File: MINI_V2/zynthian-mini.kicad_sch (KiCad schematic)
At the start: 88 parts, among them J1 NEUTRIK, J2 NEUTRIK, J3 Conn_02x04_Odd_Even, J4 Conn_01x05, J6 TRRS-PJ-320A, SW1 SW_Push, SW10 SW_Push, SW11 SW_Push, SW12 SW_Push, SW13 SW_Push, SW14 SW_Push, SW15 SW_Push, SW16 SW_Push, SW17 SW_Push, SW18 SW_Push, SW19 SW_Push, SW2 SW_Push, SW20 SW_Push, SW3 SW_Push, SW4 SW_Push, SW5 SW_Push, SW6 SW_Push, SW7 SW_Push, SW8 SW_Push, SW9 SW_Push, U1 74HCT14, U2 H11L1M

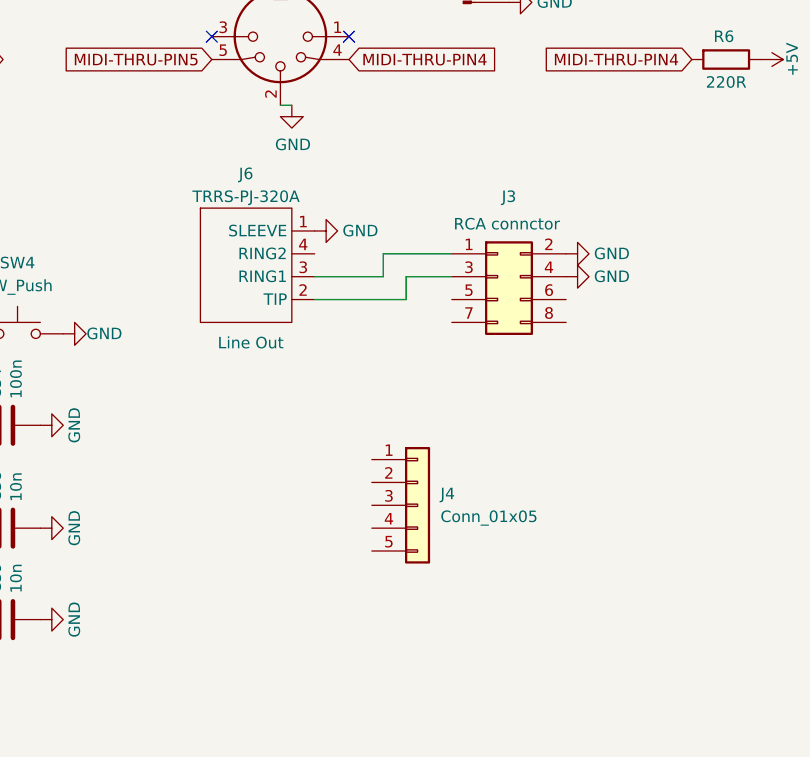
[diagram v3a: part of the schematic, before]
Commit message: small cleanup for old traces, add 2nd mini jack
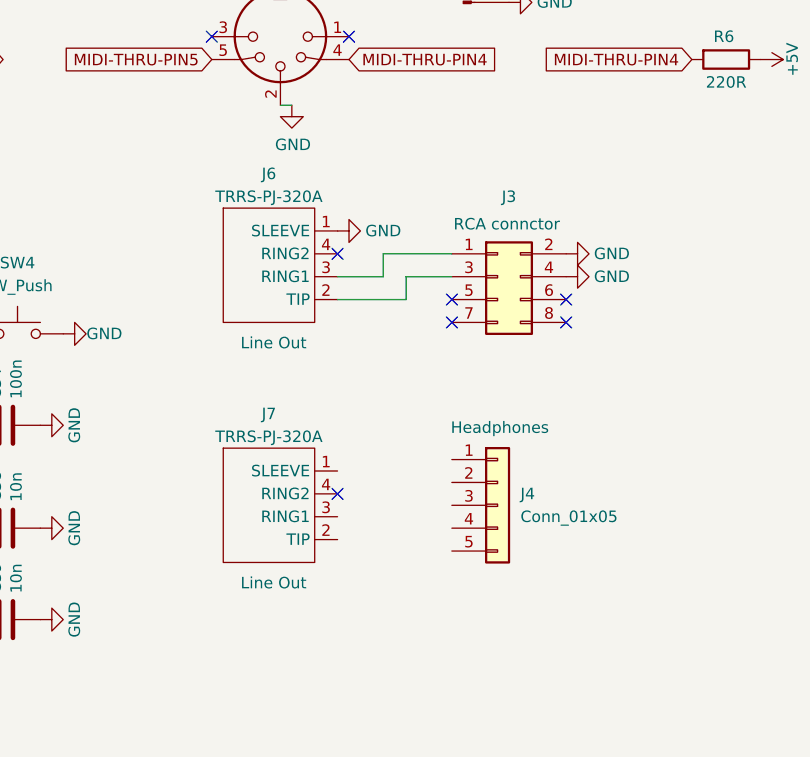
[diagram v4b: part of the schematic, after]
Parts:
- added J7: TRRS-PJ-320A, project-footprints:TRRS-PJ-320A, symbol TRRS_jack:TRRS-PJ-320A
- J4: Comment (none) -> Headphones
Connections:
- no-connect marks 15 -> 21
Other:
- moved on the sheet: J4, J6
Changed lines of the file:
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@@
 	)
 	(no_connect
+		(at 309.88 123.19)
+	)
+	(no_connect
 		(at 285.75 41.91)
 	)
@@
 	)
 	(no_connect
+		(at 322.58 123.19)
+	)
+	(no_connect
+		(at 297.18 115.57)
+	)
+	(no_connect
 		(at 22.86 160.02)
 	)
@@
 	)
 	(no_connect
+		(at 322.58 120.65)
+	)
+	(no_connect
 		(at 372.11 26.67)
 	)
 	(no_connect
+		(at 309.88 120.65)
+	)
+	(no_connect
+		(at 297.18 142.24)
+	)
+	(no_connect
 		(at 278.13 34.29)
 	)
@@
 	(wire
 		(pts
-			(xy 304.8 120.65) (xy 294.64 120.65)
+			(xy 304.8 120.65) (xy 297.18 120.65)
 		)
 		(stroke
@@
 	(wire
 		(pts
-			(xy 302.26 118.11) (xy 294.64 118.11)
+			(xy 302.26 118.11) (xy 297.18 118.11)
 		)
 		(stroke
@@
 	)
 	(symbol
+		(lib_id "TRRS_jack:TRRS-PJ-320A")
+		(at 289.56 143.51 0)
+		(unit 1)
+		(exclude_from_sim no)
+		(in_bom yes)
+		(on_board yes)
+		(dnp no)
+		(property "Reference" "J7"
+			(at 289.56 133.35 0)
+			(effects
+				(font
+					(size 1.27 1.27)
+				)
+			)
+		)
+		(property "Value" "TRRS-PJ-320A"
+			(at 289.56 135.89 0)
+			(effects
+				(font
+					(size 1.27 1.27)
+				)
+			)
+		)
+		(property "Footprint" "project-footprints:TRRS-PJ-320A"
+			(at 289.56 143.51 0)
+			(effects
+				(font
+					(size 1.27 1.27)
+				)
+				(hide yes)
+			)
+		)
+		(property "Datasheet" ""
+			(at 289.56 143.51 0)
+			(effects
+				(font
+					(size 1.27 1.27)
+				)
+				(hide yes)
+			)
+		)
+		(property "Description" ""
+			(at 289.56 143.51 0)
+			(effects
+				(font
+					(size 1.27 1.27)
+				)
+				(hide yes)
+			)
+		)
+		(property "MPN" "TRRS-PJ-320A"
+			(at 289.56 143.51 0)
+			(effects
+				(font
+					(size 1.27 1.27)
+				)
+				(hide yes)
+			)
+		)
+		(property "Link" "https://keycapsss.com/keyboard-parts/parts/54/2x-trrs-jacks-3.5mm"
+			(at 289.56 143.51 0)
+			(effects
+				(font
+					(size 1.27 1.27)
+				)
+				(hide yes)
+			)
+		)
+		(property "Comment" "Line Out"
+			(at 290.068 152.146 0)
+			(effects
+				(font
+					(size 1.27 1.27)
+				)
+			)
+		)
+		(pin "4"
+		)
+		(pin "3"
+		)
+		(pin "2"
+		)
+		(pin "1"
+		)
+		(instances
+			(project "zynthian-mini"
+				(path "/2377c5bc-c72f-48a3-b88d-9704bbbe65db"
+					(reference "J7")
+					(unit 1)
+				)
+			)
+		)
+	)
+	(symbol
 		(lib_id "power:GND")
 		(at 246.38 267.97 90)
@@
 	(symbol
 		(lib_id "TRRS_jack:TRRS-PJ-320A")
-		(at 287.02 116.84 0)
+		(at 289.56 116.84 0)
 		(unit 1)
 		(exclude_from_sim no)
@@
 		(dnp no)
 		(property "Reference" "J6"
-			(at 287.02 106.68 0)
+			(at 289.56 106.68 0)
 			(effects
 				(font
@@
 		)
 		(property "Value" "TRRS-PJ-320A"
-			(at 287.02 109.22 0)
+			(at 289.56 109.22 0)
 			(effects
 				(font
@@
 		)
 		(property "Footprint" "project-footprints:TRRS-PJ-320A"
-			(at 287.02 116.84 0)
+			(at 289.56 116.84 0)
 			(effects
 				(font
@@
 		)
 		(property "Datasheet" ""
-			(at 287.02 116.84 0)
+			(at 289.56 116.84 0)
 			(effects
 				(font
@@
 		)
 		(property "Description" ""
-			(at 287.02 116.84 0)
+			(at 289.56 116.84 0)
 			(effects
 				(font
@@
 		)
 		(property "MPN" "TRRS-PJ-320A"
-			(at 287.02 116.84 0)
+			(at 289.56 116.84 0)
 			(effects
 				(font
@@
 		)
 		(property "Link" "https://keycapsss.com/keyboard-parts/parts/54/2x-trrs-jacks-3.5mm"
-			(at 287.02 116.84 0)
+			(at 289.56 116.84 0)
 			(effects
 				(font
@@
 		)
 		(property "Comment" "Line Out"
-			(at 287.528 125.476 0)
+			(at 290.068 125.476 0)
 			(effects
 				(font
@@
 	(symbol
 		(lib_id "power:GND")
-		(at 294.64 113.03 90)
+		(at 297.18 113.03 90)
 		(mirror x)
 		(unit 1)
@@
 		(dnp no)
 		(property "Reference" "#PWR077"
-			(at 300.99 113.03 0)
+			(at 303.53 113.03 0)
 			(effects
 				(font
@@
 		)
 		(property "Value" "GND"
-			(at 299.72 113.03 90)
+			(at 302.26 113.03 90)
 			(effects
 				(font
@@
 		)
 		(property "Footprint" ""
-			(at 294.64 113.03 0)
+			(at 297.18 113.03 0)
 			(effects
 				(font
@@
 		)
 		(property "Datasheet" ""
-			(at 294.64 113.03 0)
+			(at 297.18 113.03 0)
 			(effects
 				(font
@@
 		)
 		(property "Description" "Power symbol creates a global label with name \"GND\" , ground"
-			(at 294.64 113.03 0)
+			(at 297.18 113.03 0)
 			(effects
 				(font
@@
 	(symbol
 		(lib_id "Connector_Generic:Conn_01x05")
-		(at 306.07 143.51 0)
+		(at 314.96 143.51 0)
 		(unit 1)
 		(exclude_from_sim no)
@@
 		(on_board yes)
 		(dnp no)
-		(fields_autoplaced yes)
 		(property "Reference" "J4"
-			(at 308.61 142.2399 0)
+			(at 317.5 142.2399 0)
 			(effects
 				(font
@@
 		)
 		(property "Value" "Conn_01x05"
-			(at 308.61 144.7799 0)
+			(at 317.5 144.7799 0)
 			(effects
 				(font
@@
 		)
 		(property "Footprint" "Connector_PinHeader_2.54mm:PinHeader_1x05_P2.54mm_Vertical"
-			(at 306.07 143.51 0)
+			(at 314.96 143.51 0)
 			(effects
 				(font
@@
 		)
 		(property "Datasheet" "~"
-			(at 306.07 143.51 0)
+			(at 314.96 143.51 0)
 			(effects
 				(font
@@
 		)
 		(property "Description" "Generic connector, single row, 01x05, script generated (kicad-library-utils/schlib/autogen/connector/)"
-			(at 306.07 143.51 0)
+			(at 314.96 143.51 0)
 			(effects
 				(font
@@
 			)
 		)
+		(property "Comment" "Headphones"
+			(at 315.214 134.874 0)
+			(effects
+				(font
+					(size 1.27 1.27)
+				)
+			)
+		)

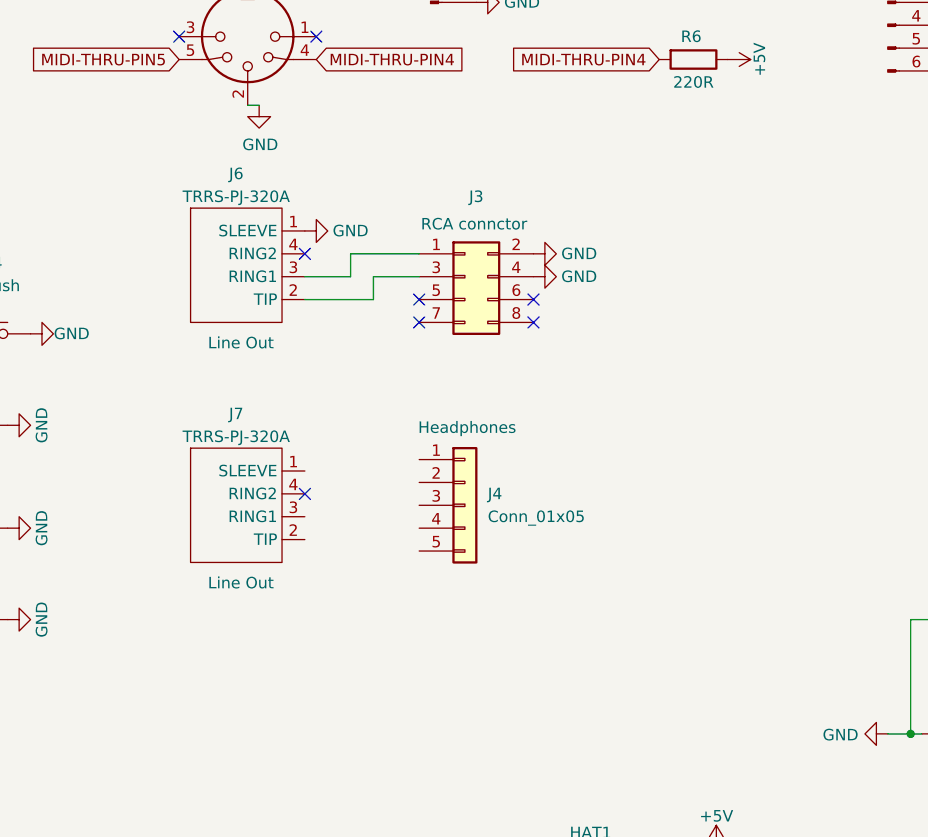
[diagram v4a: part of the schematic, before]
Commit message: finished schematic, added headphones jack
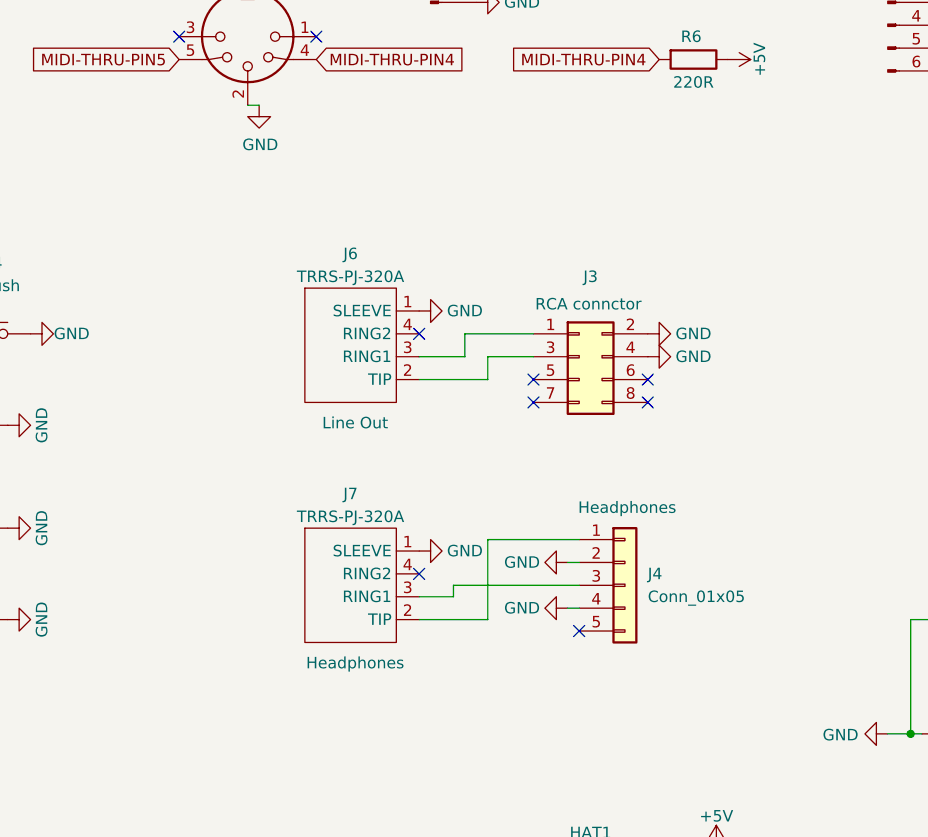
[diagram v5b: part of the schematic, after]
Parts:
- J7: Comment Line Out -> Headphones
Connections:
- net GND: now also J4.2 (Pin_2), J4.4 (Pin_4), J7.1 (SLEEVE)
- net at J7.2 (TIP): now also J4.1 (Pin_1)
- net at J7.3 (RING1): now also J4.3 (Pin_3)
- no-connect marks 21 -> 22
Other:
- moved on the sheet: J3, J4, J6, J7
